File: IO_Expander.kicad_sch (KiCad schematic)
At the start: 5 parts, among them U1901 TCA6408ARGT

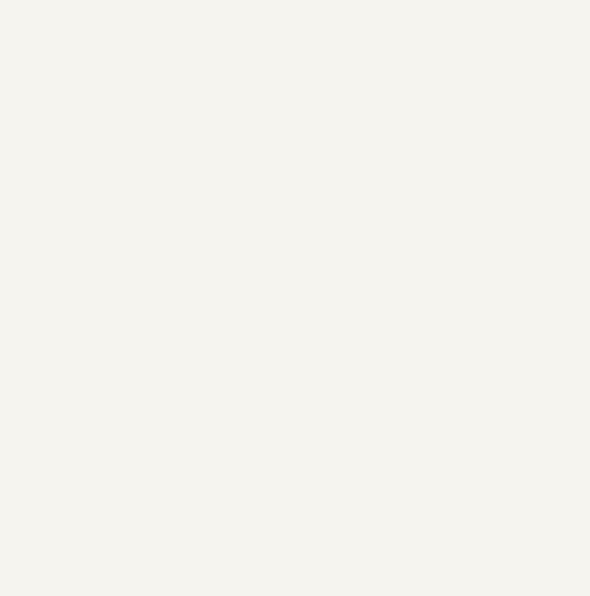
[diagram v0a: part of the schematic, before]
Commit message: added second AMUX and housekeeping
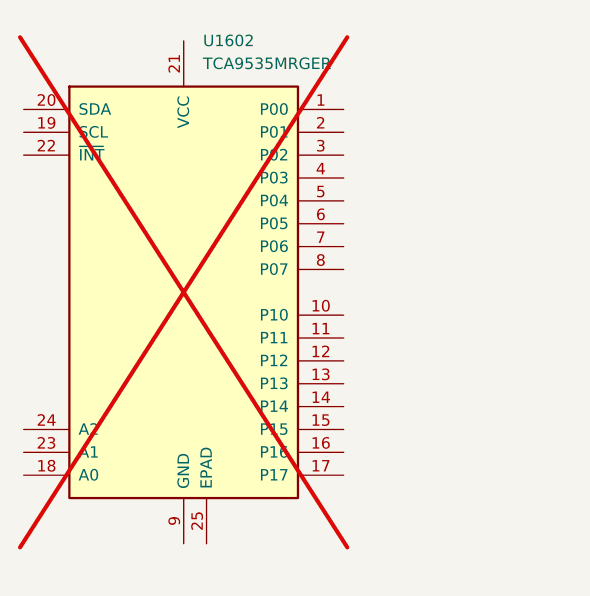
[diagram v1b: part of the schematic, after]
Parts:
- added U1602: TCA9535MRGER, Package_DFN_QFN:VQFN-24-1EP_4x4mm_P0.5mm_EP2.45x2.45mm, symbol Interface_Expansion:TCA9535MRGER
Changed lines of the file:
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@@
+	)
+	(symbol
+		(lib_id "Interface_Expansion:TCA9535MRGER")
+		(at 60.96 93.98 0)
+		(unit 1)
+		(exclude_from_sim no)
+		(in_bom no)
+		(on_board no)
+		(dnp yes)
+		(fields_autoplaced yes)
+		(property "Reference" "U1602"
+			(at 63.1033 66.04 0)
+			(effects
+				(font
+					(size 1.27 1.27)
+				)
+				(justify left)
+			)
+		)
+		(property "Value" "TCA9535MRGER"
+			(at 63.1033 68.58 0)
+			(effects
+				(font
+					(size 1.27 1.27)
+				)
+				(justify left)
+			)
+		)
+		(property "Footprint" "Package_DFN_QFN:VQFN-24-1EP_4x4mm_P0.5mm_EP2.45x2.45mm"
+			(at 91.44 119.38 0)
+			(effects
+				(font
+					(size 1.27 1.27)
+				)
+				(hide yes)
+			)
+		)
+		(property "Datasheet" "http://www.ti.com/lit/ds/symlink/tca9535.pdf"
+			(at 48.26 71.12 0)
+			(effects
+				(font
+					(size 1.27 1.27)
+				)
+				(hide yes)
+			)
+		)
+		(property "Description" "16-bit I/O expander, I2C and SMBus interface, interrupts, w/o pull-ups, QFN-24"
+			(at 60.96 93.98 0)
+			(effects
+				(font
+					(size 1.27 1.27)
+				)
+				(hide yes)
+			)
+		)
+		(pin "20"
+		)
+		(pin "24"
+		)
+		(pin "18"
+		)
+		(pin "9"
+		)
+		(pin "1"
+		)
+		(pin "19"
+		)
+		(pin "22"
+		)
+		(pin "23"
+		)
+		(pin "21"
+		)
+		(pin "25"
+		)
+		(pin "12"
+		)
+		(pin "5"
+		)
+		(pin "2"
+		)
+		(pin "8"
+		)
+		(pin "15"
+		)
+		(pin "13"
+		)
+		(pin "4"
+		)
+		(pin "3"
+		)
+		(pin "10"
+		)
+		(pin "16"
+		)
+		(pin "6"
+		)
+		(pin "17"
+		)
+		(pin "7"
+		)
+		(pin "11"
+		)
+		(pin "14"
+		)
+		(instances
+			(project ""
+				(path "/94201994-47b8-4213-8d1a-05da12b2a7b0/436fb79f-2d07-4207-b819-4d05a5fd951c/0af098ff-3966-4a58-80b4-34f2a04e28e5"
+					(reference "U6404")
+					(unit 1)
+				)
+				(path "/94201994-47b8-4213-8d1a-05da12b2a7b0/436fb79f-2d07-4207-b819-4d05a5fd951c/9df5fbc2-a6e2-42ef-8ca7-8852651bbb2a"
+					(reference "U1602")
+					(unit 1)
+				)
+			)
+		)
 	)
 	(symbol

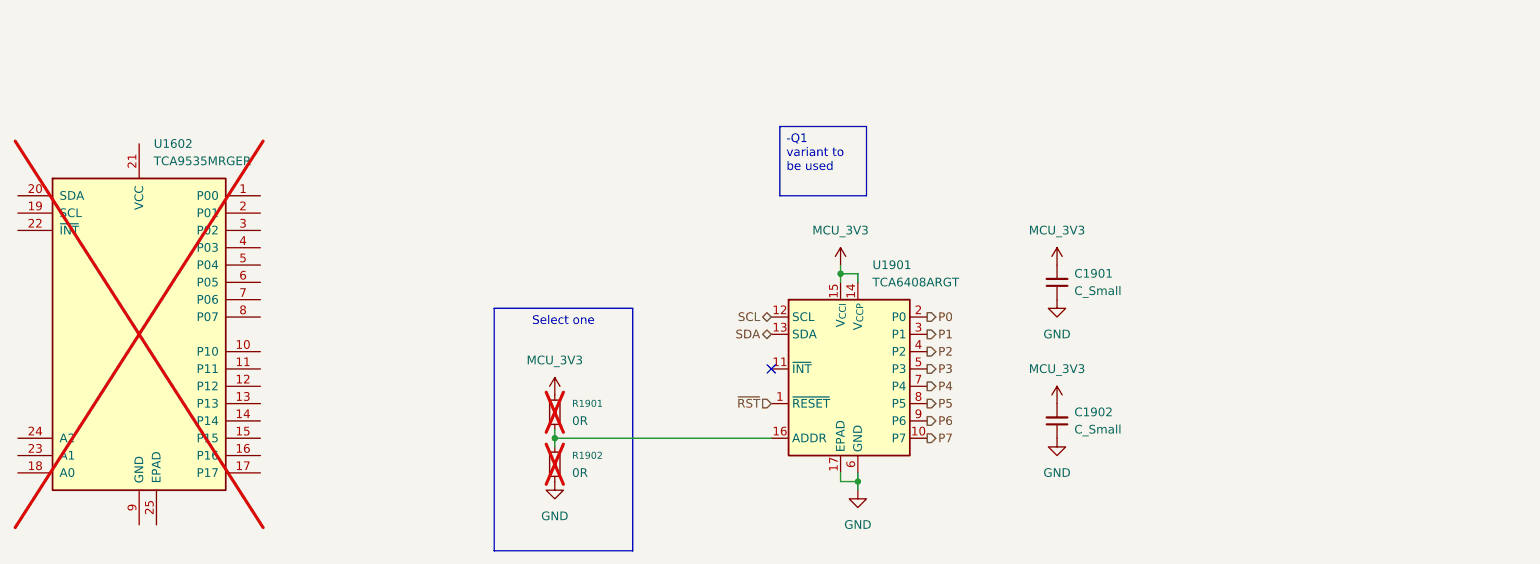
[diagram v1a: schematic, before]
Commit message: added possible solutions for mppt
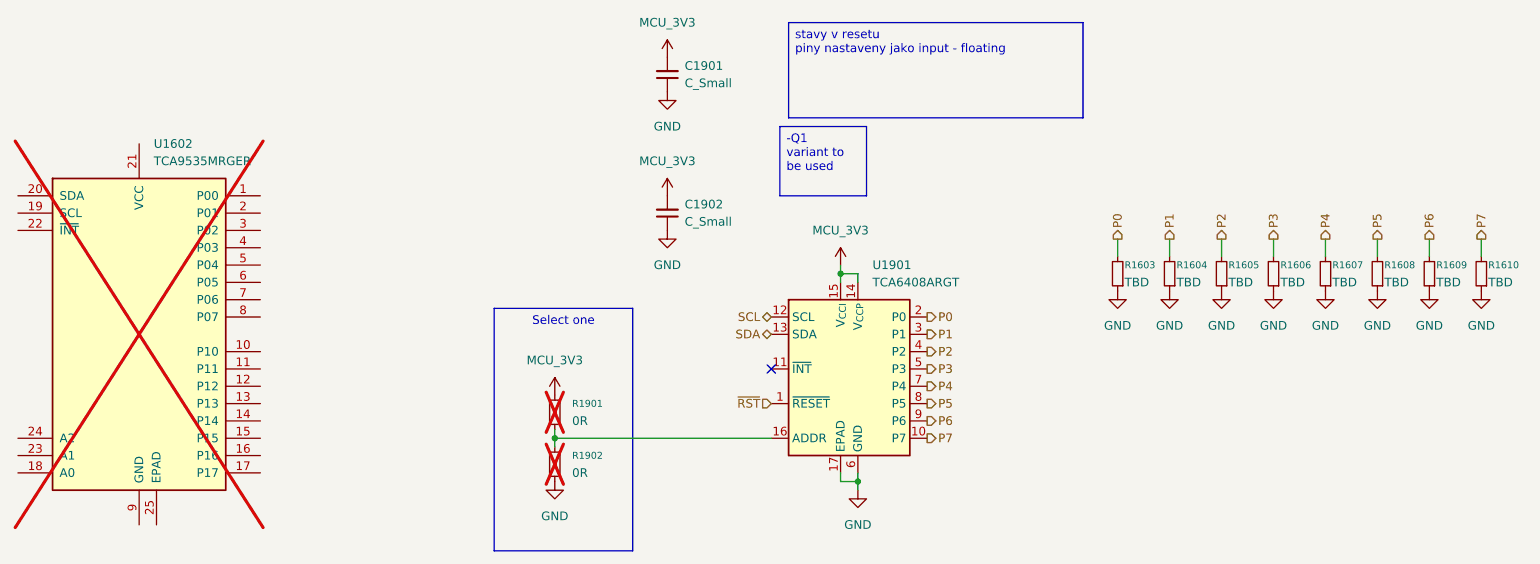
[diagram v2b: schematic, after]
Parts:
- added R1603, R1604, R1605, R1606, R1607, R1608, R1609, R1610: TBD, Resistor_SMD:R_0603_1608Metric_Pad0.98x0.95mm_HandSolder, symbol Device:R_Small
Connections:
- net GND: now also R1603.1, R1604.1, R1605.1, R1606.1, R1607.1, R1608.1, R1609.1, R1610.1
- net P0: now also R1603.2
- net P1: now also R1604.2
- net P2: now also R1605.2
- net P3: now also R1606.2
- net P4: now also R1607.2
- net P5: now also R1608.2
- net P6: now also R1609.2
- net P7: now also R1610.2
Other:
- moved on the sheet: C1901, C1902
